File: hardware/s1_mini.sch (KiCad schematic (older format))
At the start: 12 parts, among them P1 USB_Edge, U1 AP2114H, U2 SM220UF1, U3 Wemos_D1_Mini

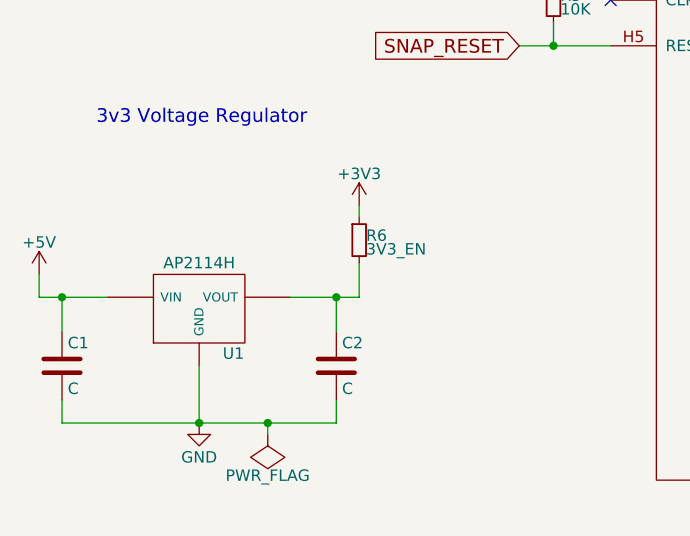
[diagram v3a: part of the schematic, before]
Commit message: Add power LED.
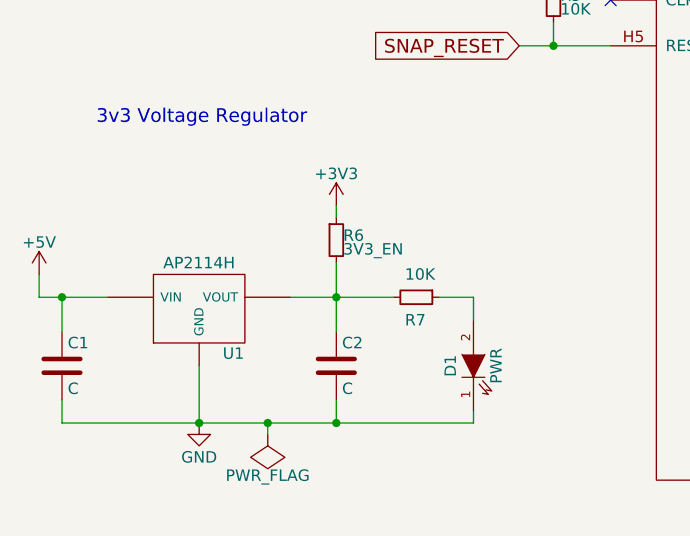
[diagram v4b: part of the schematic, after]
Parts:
- added D1: PWR, LEDs:LED_1206, symbol LED
- added R7: 10K, Resistors_SMD:R_0805_HandSoldering, symbol R_Small
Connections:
- net GND: now also D1.1 (K)
- net at C2.1, R6.2, U1.2 (VOUT): now also R7.2
- new net: D1.2 (A), R7.1
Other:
- moved on the sheet: R6
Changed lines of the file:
@@
 EESchema Schematic File Version 2
-LIBS:s1_mini-rescue
 LIBS:crumpschemes
 LIBS:power
@@
 $EndComp
 $Comp
-L GND #PWR4
+L GND #PWR01
 U 1 1 57C52ED6
 P 3000 5250
-F 0 "#PWR4" H 3000 5000 50  0001 C CNN
+F 0 "#PWR01" H 3000 5000 50  0001 C CNN
 F 1 "GND" H 3000 5100 50  0000 C CNN
 F 2 "" H 3000 5250 50  0000 C CNN
@@
 	2400 5150 2400 5250
 Wire Wire Line
-	2400 5250 3600 5250
+	2400 5250 4200 5250
 Wire Wire Line
 	3000 5000 3000 5250
@@
 	2300 4700 2600 4700
 Wire Wire Line
-	3600 4850 3600 4700
-Wire Wire Line
-	3700 4700 3400 4700
-$Comp
-L +5V #PWR1
+	3600 4550 3600 4850
+Wire Wire Line
+	3400 4700 3850 4700
+$Comp
+L +5V #PWR02
 U 1 1 57C52F3A
 P 2300 4600
-F 0 "#PWR1" H 2300 4450 50  0001 C CNN
+F 0 "#PWR02" H 2300 4450 50  0001 C CNN
 F 1 "+5V" H 2300 4740 50  0000 C CNN
 F 2 "" H 2300 4600 50  0000 C CNN
@@
 $EndComp
 $Comp
-L +3V3 #PWR5
+L +3V3 #PWR03
 U 1 1 57C52F76
-P 3700 4300
-F 0 "#PWR5" H 3700 4150 50  0001 C CNN
-F 1 "+3V3" H 3700 4440 50  0000 C CNN
-F 2 "" H 3700 4300 50  0000 C CNN
-F 3 "" H 3700 4300 50  0000 C CNN
-	1    3700 4300
+P 3600 4300
+F 0 "#PWR03" H 3600 4150 50  0001 C CNN
+F 1 "+3V3" H 3600 4440 50  0000 C CNN
+F 2 "" H 3600 4300 50  0000 C CNN
+F 3 "" H 3600 4300 50  0000 C CNN
+	1    3600 4300
 	1    0    0    -1
 $EndComp
@@
 	2300 4600 2300 4700
 Connection ~ 2400 4700
-Wire Wire Line
-	3700 4550 3700 4700
 Connection ~ 3600 4700
 $Comp
-L +5V #PWR2
+L +5V #PWR04
 U 1 1 57C53068
 P 2750 2650
-F 0 "#PWR2" H 2750 2500 50  0001 C CNN
+F 0 "#PWR04" H 2750 2500 50  0001 C CNN
 F 1 "+5V" H 2750 2790 50  0000 C CNN
 F 2 "" H 2750 2650 50  0000 C CNN
@@
 	2750 2700 2750 2650
 $Comp
-L GND #PWR3
+L GND #PWR05
 U 1 1 57C531D5
 P 2750 3050
-F 0 "#PWR3" H 2750 2800 50  0001 C CNN
+F 0 "#PWR05" H 2750 2800 50  0001 C CNN
 F 1 "GND" H 2750 2900 50  0000 C CNN
 F 2 "" H 2750 3050 50  0000 C CNN
@@
 NoConn ~ 2850 2900
 $Comp
-L +3V3 #PWR6
+L +3V3 #PWR06
 U 1 1 57C5338E
 P 4500 2850
-F 0 "#PWR6" H 4500 2700 50  0001 C CNN
+F 0 "#PWR06" H 4500 2700 50  0001 C CNN
 F 1 "+3V3" H 4500 2990 50  0000 C CNN
 F 2 "" H 4500 2850 50  0000 C CNN
@@
 Connection ~ 4750 2000
 $Comp
-L GND #PWR7
+L GND #PWR07
 U 1 1 57C5360C
 P 4550 2250
-F 0 "#PWR7" H 4550 2000 50  0001 C CNN
+F 0 "#PWR07" H 4550 2000 50  0001 C CNN
 F 1 "GND" H 4550 2100 50  0000 C CNN
 F 2 "" H 4550 2250 50  0000 C CNN
@@
 	8450 2900 8500 2900
 $Comp
-L +3V3 #PWR8
+L +3V3 #PWR08
 U 1 1 57C55CE8
 P 8450 3100
-F 0 "#PWR8" H 8450 2950 50  0001 C CNN
+F 0 "#PWR08" H 8450 2950 50  0001 C CNN
 F 1 "+3V3" H 8450 3240 50  0000 C CNN
 F 2 "" H 8450 3100 50  0000 C CNN
@@
 $EndComp
 $Comp
-L +5V #PWR9
+L +5V #PWR09
 U 1 1 57C55E11
 P 9650 3100
-F 0 "#PWR9" H 9650 2950 50  0001 C CNN
+F 0 "#PWR09" H 9650 2950 50  0001 C CNN
 F 1 "+5V" H 9650 3240 50  0000 C CNN
 F 2 "" H 9650 3100 50  0000 C CNN
@@
 $EndComp
 $Comp
-L GND #PWR10
+L GND #PWR010
 U 1 1 57C55E21
 P 9900 3100
-F 0 "#PWR10" H 9900 2850 50  0001 C CNN
+F 0 "#PWR010" H 9900 2850 50  0001 C CNN
 F 1 "GND" H 9900 2950 50  0000 C CNN
 F 2 "" H 9900 3100 50  0000 C CNN
@@
 Connection ~ 4550 3000
 $Comp
-L PWR_FLAG #FLG1
+L PWR_FLAG #FLG011
 U 1 1 57C589B0
 P 3300 5300
-F 0 "#FLG1" H 3300 5395 50  0001 C CNN
+F 0 "#FLG011" H 3300 5395 50  0001 C CNN
 F 1 "PWR_FLAG" H 3300 5480 50  0000 C CNN
 F 2 "" H 3300 5300 50  0000 C CNN
@@
 L R_Small R6
 U 1 1 57C62FB9
-P 3700 4450
-F 0 "R6" H 3730 4470 50  0000 L CNN
-F 1 "3V3_EN" H 3730 4410 50  0000 L CNN
-F 2 "Resistors_SMD:R_0805_HandSoldering" H 3700 4450 50  0001 C CNN
-F 3 "" H 3700 4450 50  0000 C CNN
-	1    3700 4450
-	1    0    0    -1
-$EndComp
-Wire Wire Line
-	3700 4350 3700 4300
-$Comp
-L PWR_FLAG #FLG2
+P 3600 4450
+F 0 "R6" H 3630 4470 50  0000 L CNN
+F 1 "3V3_EN" H 3630 4410 50  0000 L CNN
+F 2 "Resistors_SMD:R_0805_HandSoldering" H 3600 4450 50  0001 C CNN
+F 3 "" H 3600 4450 50  0000 C CNN
+	1    3600 4450
+	1    0    0    -1
+$EndComp
+Wire Wire Line
+	3600 4350 3600 4300
+$Comp
+L PWR_FLAG #FLG012
 U 1 1 57C63CE4
 P 8650 3250
-F 0 "#FLG2" H 8650 3345 50  0001 C CNN
+F 0 "#FLG012" H 8650 3345 50  0001 C CNN
 F 1 "PWR_FLAG" H 8650 3430 50  0000 C CNN
 F 2 "" H 8650 3250 50  0000 C CNN
@@
 	1    0    0    -1
 $EndComp
+$Comp
+L LED D1
+U 1 1 57C64BE0
+P 4200 5000
+F 0 "D1" H 4200 5100 50  0000 C CNN
+F 1 "PWR" H 4200 4900 50  0000 C CNN
+F 2 "LEDs:LED_1206" H 4200 5000 50  0001 C CNN
+F 3 "" H 4200 5000 50  0000 C CNN
+	1    4200 5000
+	0    -1   -1   0
+$EndComp
+$Comp
+L R_Small R7
+U 1 1 57C64CC4
+P 3950 4700
+F 0 "R7" V 4050 4650 50  0000 L CNN
+F 1 "10K" V 3850 4650 50  0000 L CNN
+F 2 "Resistors_SMD:R_0805_HandSoldering" H 3950 4700 50  0001 C CNN
+F 3 "" H 3950 4700 50  0000 C CNN
+	1    3950 4700
+	0    1    1    0
+$EndComp
+Wire Wire Line
+	4050 4700 4200 4700
+Wire Wire Line
+	4200 4700 4200 4800
+Wire Wire Line
+	4200 5250 4200 5200
+Connection ~ 3600 5250
 $EndSCHEMATC

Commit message: Route and finish up board.
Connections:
- net +3V3: now also R7.2
- net at C2.1, R6.2, U1.2 (VOUT): no longer R7.2
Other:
- moved on the sheet: D1, R7
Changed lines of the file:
@@
 	2400 5150 2400 5250
-Wire Wire Line
-	2400 5250 4200 5250
 Wire Wire Line
 	3000 5000 3000 5250
@@
 Wire Wire Line
 	3600 4550 3600 4850
-Wire Wire Line
-	3400 4700 3850 4700
 $Comp
 L +5V #PWR02
@@
 	4500 3000 4800 3000
 Wire Wire Line
-	4500 2900 4800 2900
+	4100 2900 4800 2900
 Connection ~ 4500 2900
 Wire Wire Line
@@
 	4550 2250 4550 2200
 Wire Wire Line
-	4550 2200 4750 2200
+	4100 2200 4750 2200
 Connection ~ 4750 2200
 Wire Wire Line
@@
 L LED D1
 U 1 1 57C64BE0
-P 4200 5000
-F 0 "D1" H 4200 5100 50  0000 C CNN
-F 1 "PWR" H 4200 4900 50  0000 C CNN
-F 2 "LEDs:LED_1206" H 4200 5000 50  0001 C CNN
-F 3 "" H 4200 5000 50  0000 C CNN
-	1    4200 5000
-	0    -1   -1   0
+P 4100 2450
+F 0 "D1" H 4100 2550 50  0000 C CNN
+F 1 "PWR" H 4100 2350 50  0000 C CNN
+F 2 "LEDs:LED_1206" H 4100 2450 50  0001 C CNN
+F 3 "" H 4100 2450 50  0000 C CNN
+	1    4100 2450
+	0    1    1    0
 $EndComp
 $Comp
 L R_Small R7
 U 1 1 57C64CC4
-P 3950 4700
-F 0 "R7" V 4050 4650 50  0000 L CNN
-F 1 "10K" V 3850 4650 50  0000 L CNN
-F 2 "Resistors_SMD:R_0805_HandSoldering" H 3950 4700 50  0001 C CNN
-F 3 "" H 3950 4700 50  0000 C CNN
-	1    3950 4700
-	0    1    1    0
-$EndComp
-Wire Wire Line
-	4050 4700 4200 4700
-Wire Wire Line
-	4200 4700 4200 4800
-Wire Wire Line
-	4200 5250 4200 5200
+P 4100 2800
+F 0 "R7" V 4200 2750 50  0000 L CNN
+F 1 "10K" V 4000 2750 50  0000 L CNN
+F 2 "Resistors_SMD:R_0805_HandSoldering" H 4100 2800 50  0001 C CNN
+F 3 "" H 4100 2800 50  0000 C CNN
+	1    4100 2800
+	1    0    0    -1
+$EndComp
 Connection ~ 3600 5250
+Wire Wire Line
+	3400 4700 3600 4700
+Wire Wire Line
+	2400 5250 3600 5250
+Wire Wire Line
+	4100 2700 4100 2650
+Wire Wire Line
+	4100 2250 4100 2200
+Connection ~ 4550 2200
 $EndSCHEMATC
